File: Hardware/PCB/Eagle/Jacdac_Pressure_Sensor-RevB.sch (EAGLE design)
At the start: 29 parts, among them IC1 LPS33HWTR, IC2 STM32G030F6P6, J1 JD, J2 PWR, J3 GND, J4 GND, J5 HACK-CONNECT-5, U1 XC6206

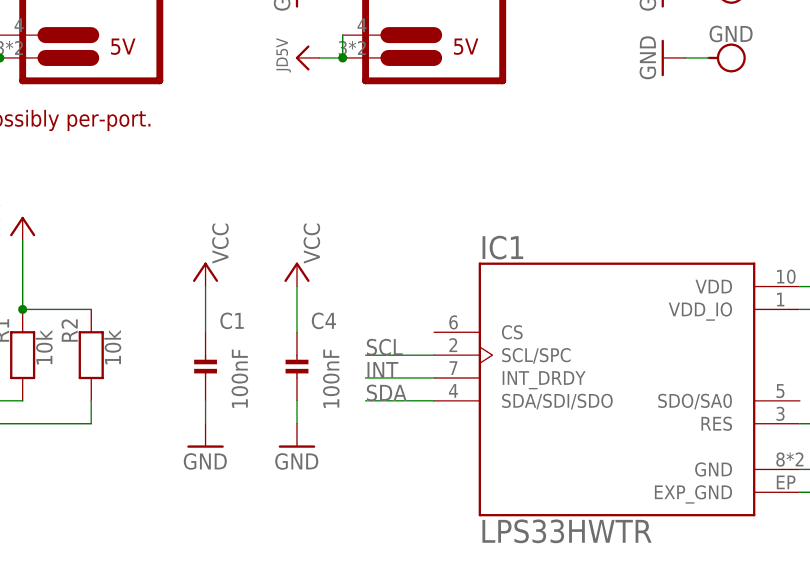
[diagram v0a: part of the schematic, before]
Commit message: Updated design : Added CS trace
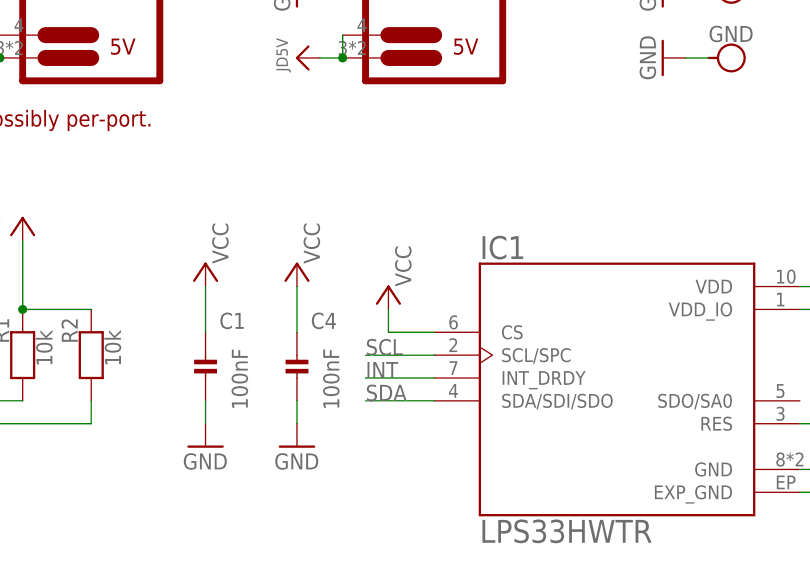
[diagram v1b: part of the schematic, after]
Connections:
- net VCC: now also IC1.CS
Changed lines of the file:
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@@
 <part name="LABEL_LOGO2" library="MMC Eagle" library_urn="urn:adsk.eagle:library:13126479" deviceset="MMC_LOGO-" device="XSM" package3d_urn="urn:adsk.eagle:package:36433256/2"/>
 <part name="FRAME1" library="frames" library_urn="urn:adsk.eagle:library:229" deviceset="A4L-LOC" device=""/>
+<part name="P+3" library="milador" library_urn="urn:adsk.eagle:library:12595918" deviceset="VCC" device=""/>
 </parts>
 <sheets>
@@
 <attribute name="LAST_DATE_TIME" x="54.61" y="-45.72" size="2.286" layer="94"/>
 <attribute name="SHEET" x="67.945" y="-50.8" size="2.54" layer="94"/>
+</instance>
+<instance part="P+3" gate="VCC" x="12.7" y="50.8" smashed="yes">
+<attribute name="VALUE" x="15.24" y="50.8" size="1.778" layer="96" rot="R90"/>
 </instance>
 </instances>
@@
 <junction x="66.04" y="50.8"/>
 </segment>
+<segment>
+<pinref part="IC1" gate="G$1" pin="CS"/>
+<pinref part="P+3" gate="VCC" pin="VCC"/>
+<wire x1="17.78" y1="45.72" x2="12.7" y2="45.72" width="0.1524" layer="91"/>
+<wire x1="12.7" y1="45.72" x2="12.7" y2="48.26" width="0.1524" layer="91"/>
+</segment>
 </net>

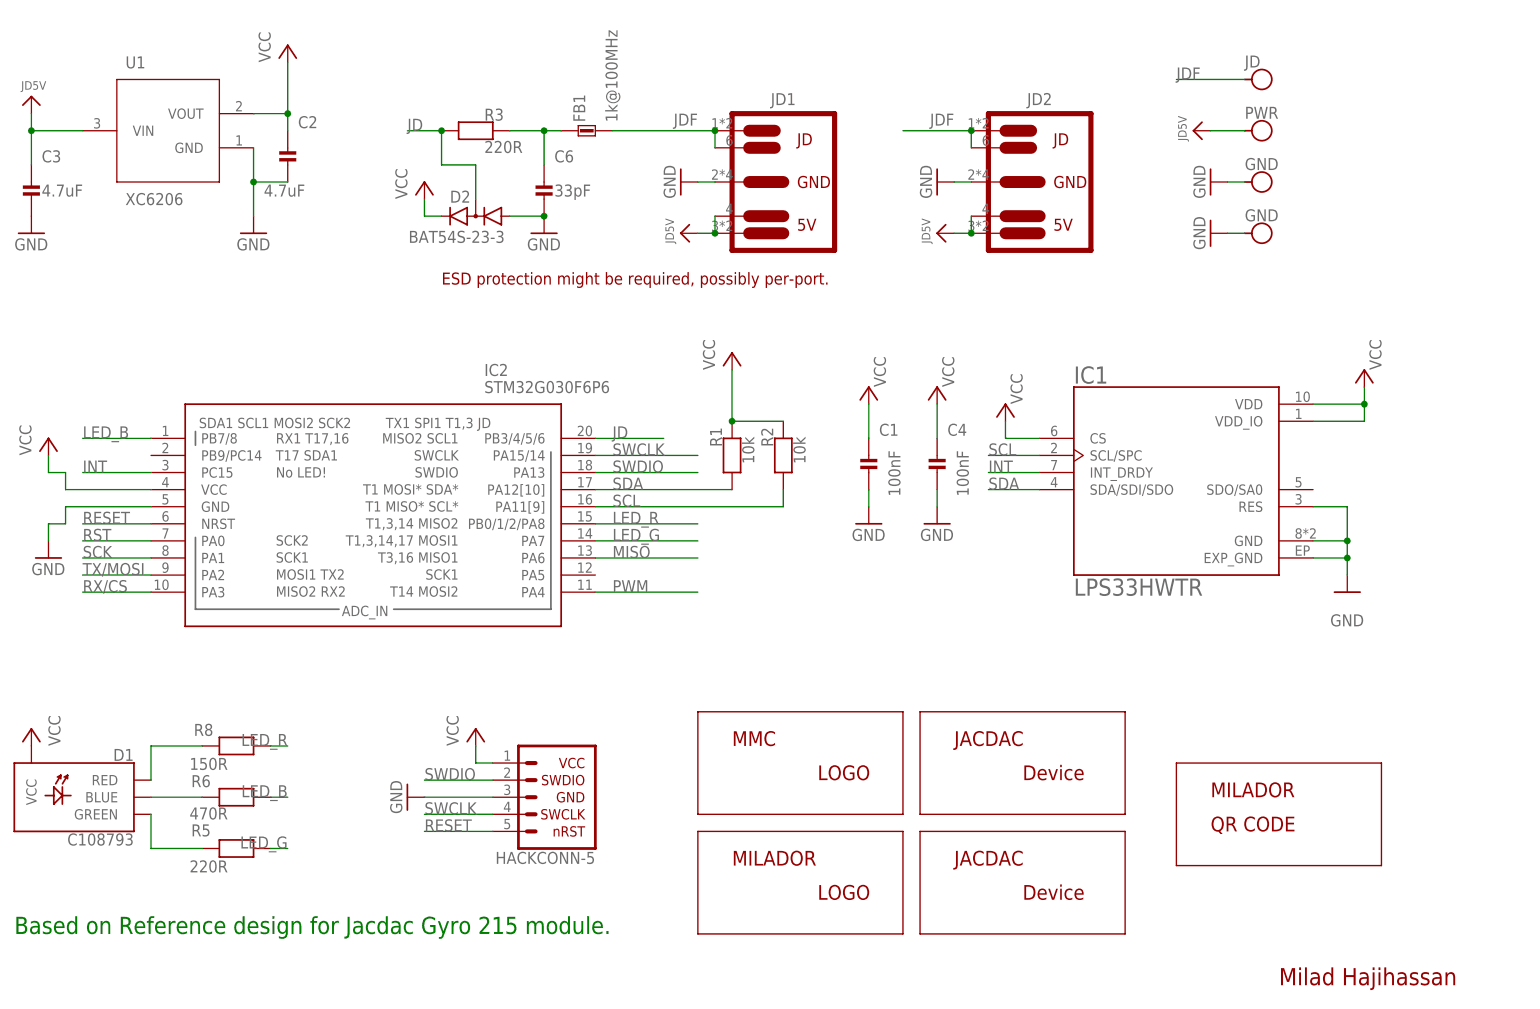
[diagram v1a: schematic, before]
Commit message: Updated RevB : Added Pull-Up to SA0
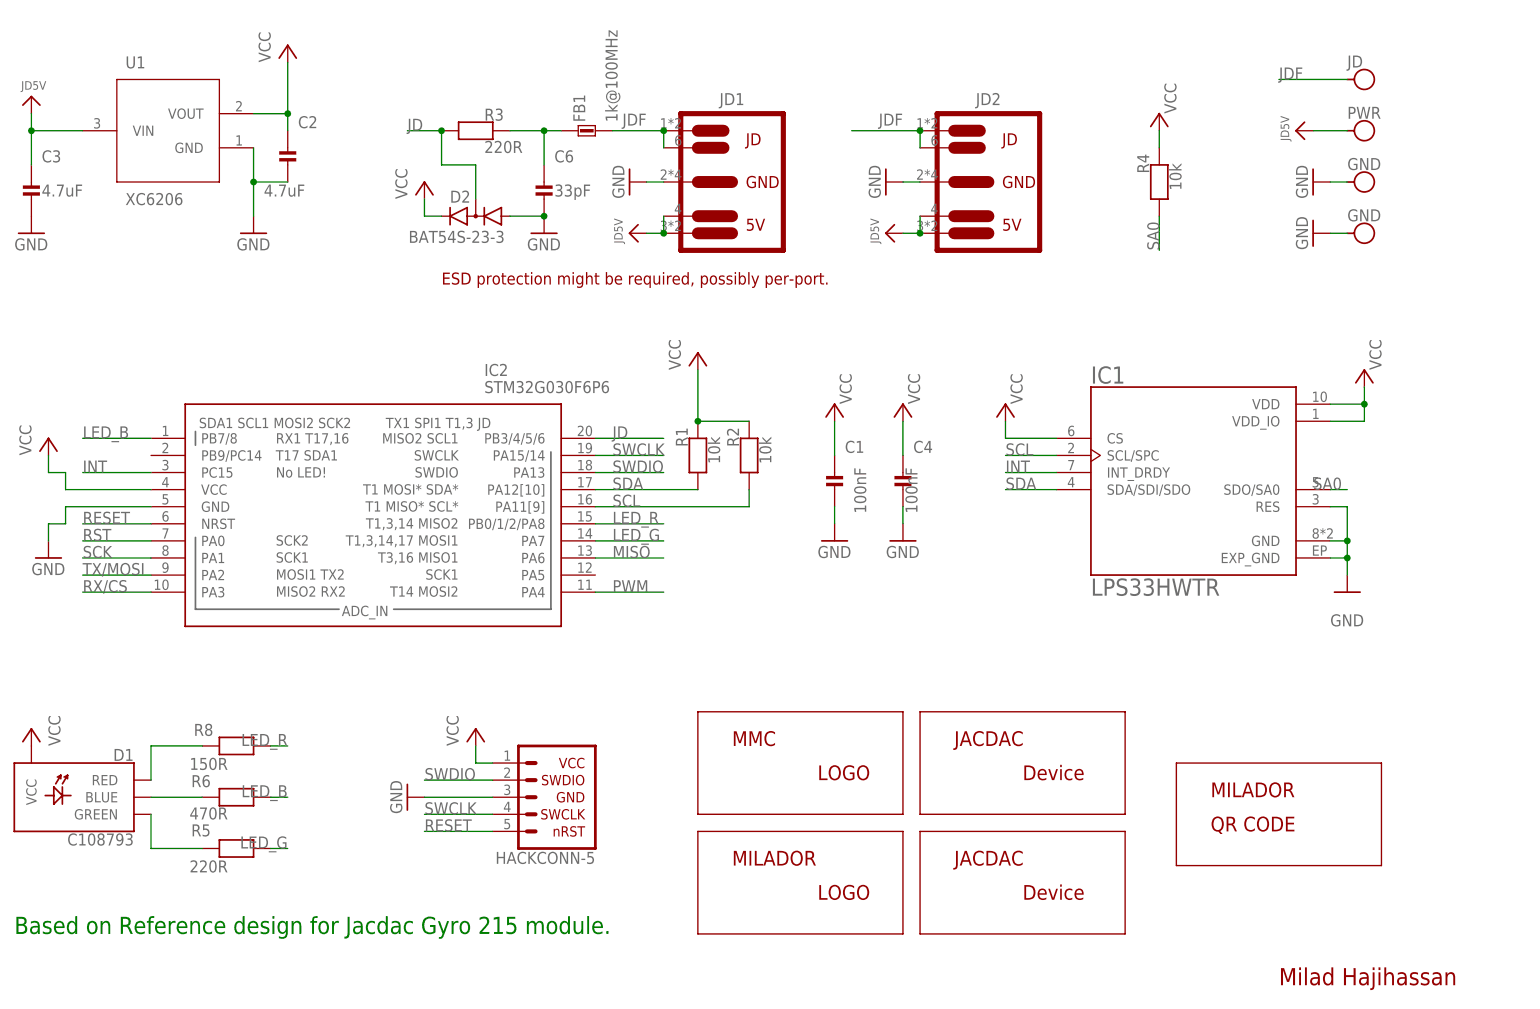
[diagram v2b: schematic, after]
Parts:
- added R4: 10k, milador_SMD:RESISTOR-0402
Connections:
- new net SA0: IC1.SDO/SA0, R4.1
- net VCC: now also R4.2
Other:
- moved on the sheet: C1, C4, IC1, JD1, JD2, R1, R2
